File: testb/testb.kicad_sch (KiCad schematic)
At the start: 3 parts

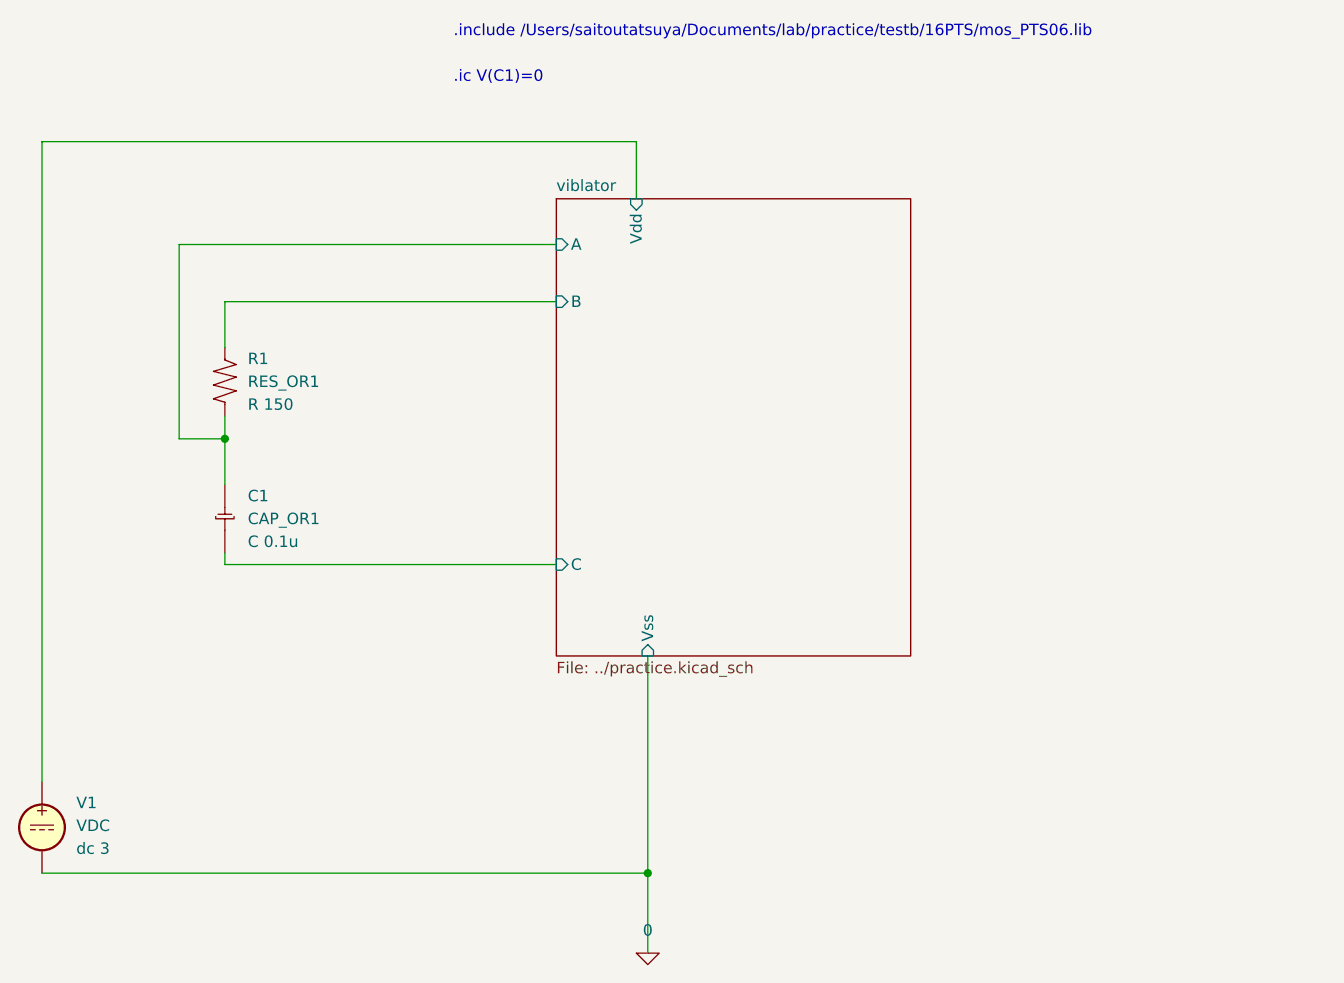
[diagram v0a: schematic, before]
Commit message: 入出力点を双方向に変更
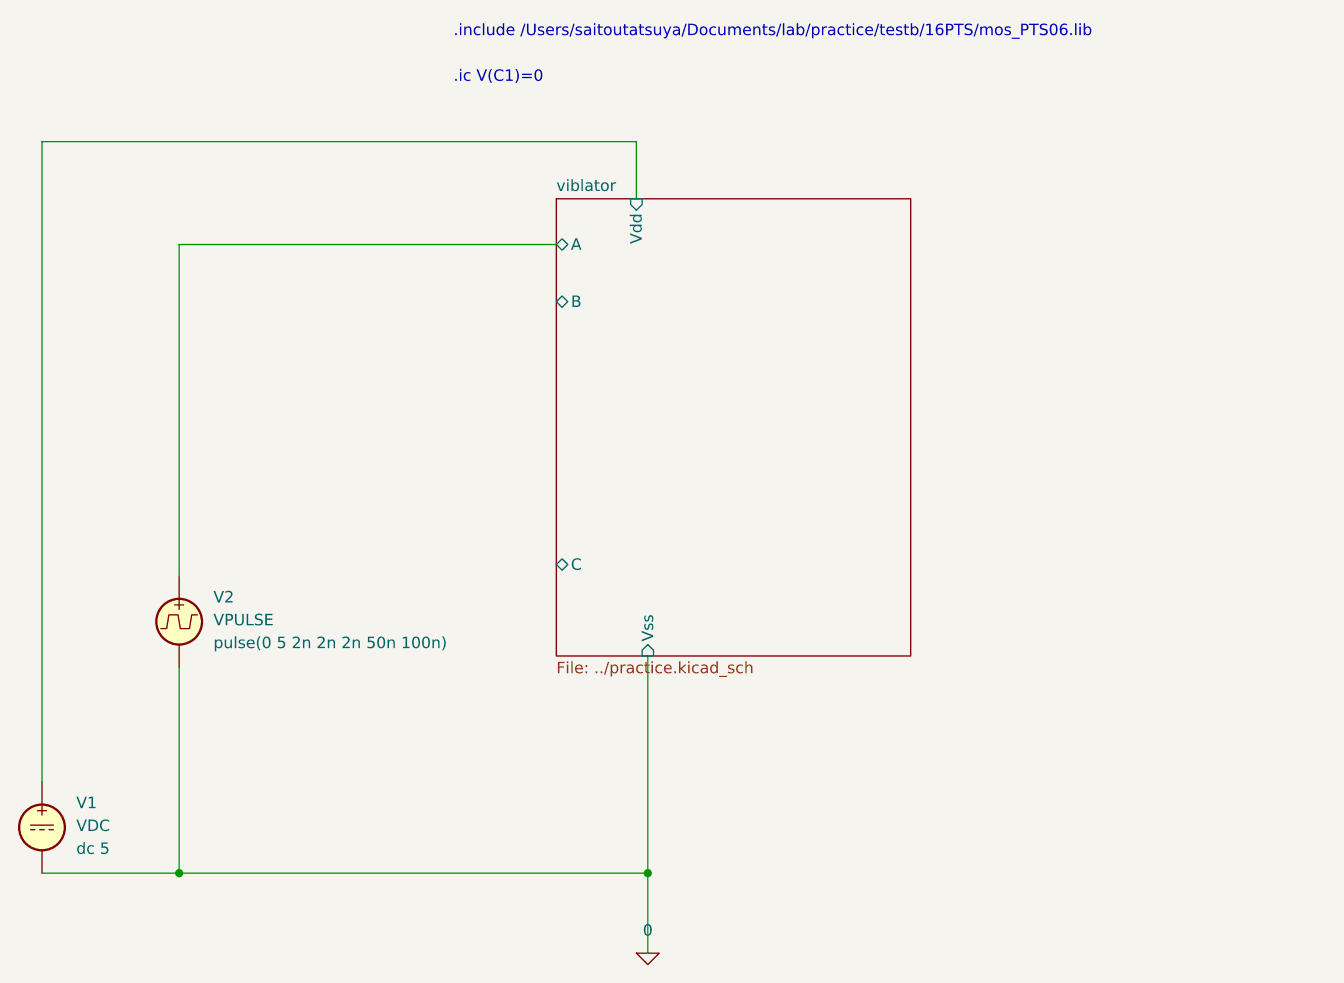
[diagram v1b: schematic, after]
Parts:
- removed C1: CAP_OR1, symbol 0_OR1Symbols:CAP_OR1
- removed R1: RES_OR1, symbol 0_OR1Symbols:RES_OR1
- added V2: VPULSE, symbol Simulation_SPICE:VPULSE
- V1: Spice_Model dc 3 -> dc 5
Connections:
- net 0: now also V2.2
- net viblator/A: now also V2.1
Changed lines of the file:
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@@
   (junction (at 152.4 129.54) (diameter 0) (color 0 0 0 0)
   )
-  (junction (at 105.41 81.28) (diameter 0) (color 0 0 0 0)
+  (junction (at 100.33 129.54) (diameter 0) (color 0 0 0 0)
   )
-  (wire (pts (xy 105.41 95.25) (xy 142.24 95.25))
+  (wire (pts (xy 100.33 106.68) (xy 100.33 129.54))
     (stroke (width 0) (type default) (color 0 0 0 0))
   )
@@
     (stroke (width 0) (type default) (color 0 0 0 0))
   )
-  (wire (pts (xy 152.4 129.54) (xy 152.4 138.43))
+  (wire (pts (xy 100.33 129.54) (xy 152.4 129.54))
     (stroke (width 0) (type default) (color 0 0 0 0))
   )
-  (wire (pts (xy 105.41 66.04) (xy 142.24 66.04))
-    (stroke (width 0) (type default) (color 0 0 0 0))
-  )
-  (wire (pts (xy 100.33 59.69) (xy 100.33 81.28))
+  (wire (pts (xy 152.4 129.54) (xy 152.4 138.43))
     (stroke (width 0) (type default) (color 0 0 0 0))
   )
@@
     (stroke (width 0) (type default) (color 0 0 0 0))
   )
-  (wire (pts (xy 100.33 59.69) (xy 142.24 59.69))
-    (stroke (width 0) (type default) (color 0 0 0 0))
-  )
   (wire (pts (xy 151.13 48.26) (xy 151.13 54.61))
     (stroke (width 0) (type default) (color 0 0 0 0))
   )
-  (wire (pts (xy 105.41 78.74) (xy 105.41 81.28))
+  (wire (pts (xy 85.09 129.54) (xy 100.33 129.54))
     (stroke (width 0) (type default) (color 0 0 0 0))
   )
-  (wire (pts (xy 85.09 129.54) (xy 152.4 129.54))
-    (stroke (width 0) (type default) (color 0 0 0 0))
-  )
-  (wire (pts (xy 105.41 93.98) (xy 105.41 95.25))
-    (stroke (width 0) (type default) (color 0 0 0 0))
-  )
-  (wire (pts (xy 105.41 81.28) (xy 105.41 86.36))
-    (stroke (width 0) (type default) (color 0 0 0 0))
-  )
-  (wire (pts (xy 100.33 81.28) (xy 105.41 81.28))
+  (wire (pts (xy 100.33 96.52) (xy 100.33 59.69))
     (stroke (width 0) (type default) (color 0 0 0 0))
   )
@@
     (stroke (width 0) (type default) (color 0 0 0 0))
   )
-  (wire (pts (xy 105.41 66.04) (xy 105.41 71.12))
+  (wire (pts (xy 100.33 59.69) (xy 142.24 59.69))
     (stroke (width 0) (type default) (color 0 0 0 0))
   )
@@
     (pin "1")
   )
-  (symbol (lib_id "0_OR1Symbols:RES_OR1") (at 105.41 71.12 0) (unit 1)
+  (symbol (lib_id "Simulation_SPICE:VPULSE") (at 100.33 101.6 0) (unit 1)
     (in_bom yes) (on_board yes) (fields_autoplaced)
-    (property "Reference" "R1" (id 0) (at 107.95 72.3899 0)
+    (property "Reference" "V2" (id 0) (at 104.14 98.8701 0)
       (effects (font (size 1.27 1.27)) (justify left))
     )
-    (property "Value" "RES_OR1" (id 1) (at 107.95 74.9299 0)
+    (property "Value" "VPULSE" (id 1) (at 104.14 101.4101 0)
       (effects (font (size 1.27 1.27)) (justify left))
     )
-    (property "Footprint" "" (id 2) (at 106.68 71.12 0)
+    (property "Footprint" "" (id 2) (at 100.33 101.6 0)
       (effects (font (size 1.27 1.27)) hide)
     )
-    (property "Datasheet" "" (id 3) (at 106.68 71.12 0)
+    (property "Datasheet" "~" (id 3) (at 100.33 101.6 0)
       (effects (font (size 1.27 1.27)) hide)
     )
-    (property "Spice_Primitive" "R" (id 4) (at 109.22 80.01 0)
+    (property "Spice_Netlist_Enabled" "Y" (id 4) (at 100.33 101.6 0)
       (effects (font (size 1.27 1.27)) (justify left) hide)
     )
-    (property "Spice_Model" "R 150" (id 5) (at 107.95 77.4699 0)
+    (property "Spice_Primitive" "V" (id 5) (at 100.33 101.6 0)
+      (effects (font (size 1.27 1.27)) (justify left) hide)
+    )
+    (property "Spice_Model" "pulse(0 5 2n 2n 2n 50n 100n)" (id 6) (at 104.14 103.9501 0)
       (effects (font (size 1.27 1.27)) (justify left))
-    )
-    (property "Spice_Netlist_Enabled" "Y" (id 6) (at 109.22 77.47 0)
-      (effects (font (size 1.27 1.27)) (justify left) hide)
     )
     (pin "1")
@@
       (effects (font (size 1.27 1.27)) (justify left) hide)
     )
-    (property "Spice_Model" "dc 3" (id 6) (at 88.9 126.8101 0)
+    (property "Spice_Model" "dc 5" (id 6) (at 88.9 126.8101 0)
       (effects (font (size 1.27 1.27)) (justify left))
-    )
-    (pin "1")
-    (pin "2")
-  )
-  (symbol (lib_id "0_OR1Symbols:CAP_OR1") (at 105.41 86.36 0) (unit 1)
-    (in_bom yes) (on_board yes) (fields_autoplaced)
-    (property "Reference" "C1" (id 0) (at 107.95 87.6299 0)
-      (effects (font (size 1.27 1.27)) (justify left))
-    )
-    (property "Value" "CAP_OR1" (id 1) (at 107.95 90.1699 0)
-      (effects (font (size 1.27 1.27)) (justify left))
-    )
-    (property "Footprint" "" (id 2) (at 104.14 84.582 0)
-      (effects (font (size 1.27 1.27)) hide)
-    )
-    (property "Datasheet" "" (id 3) (at 104.14 84.582 0)
-      (effects (font (size 1.27 1.27)) hide)
-    )
-    (property "Spice_Primitive" "C" (id 4) (at 107.95 96.52 0)
-      (effects (font (size 1.27 1.27)) (justify left) hide)
-    )
-    (property "Spice_Model" "C 0.1u" (id 5) (at 107.95 92.7099 0)
-      (effects (font (size 1.27 1.27)) (justify left))
-    )
-    (property "Spice_Netlist_Enabled" "Y" (id 6) (at 107.95 93.98 0)
-      (effects (font (size 1.27 1.27)) (justify left) hide)
     )
     (pin "1")
@@
       (effects (font (size 1.27 1.27)) (justify left top))
     )
-    (pin "A" input (at 142.24 59.69 180)
-      (effects (font (size 1.27 1.27)) (justify left))
-    )
     (pin "Vdd" input (at 151.13 54.61 90)
       (effects (font (size 1.27 1.27)) (justify right))
-    )
-    (pin "B" input (at 142.24 66.04 180)
-      (effects (font (size 1.27 1.27)) (justify left))
     )
     (pin "Vss" input (at 152.4 105.41 270)
       (effects (font (size 1.27 1.27)) (justify left))
     )
-    (pin "C" input (at 142.24 95.25 180)
+    (pin "A" bidirectional (at 142.24 59.69 180)
+      (effects (font (size 1.27 1.27)) (justify left))
+    )
+    (pin "B" bidirectional (at 142.24 66.04 180)
+      (effects (font (size 1.27 1.27)) (justify left))
+    )
+    (pin "C" bidirectional (at 142.24 95.25 180)
       (effects (font (size 1.27 1.27)) (justify left))
     )
@@
     (path "/03533d21-8bf4-4e20-a4f6-d9e08c36312e"
       (reference "#GND01") (unit 1) (value "0") (footprint "")
-    )
-    (path "/e7907c5a-8ef1-42da-b288-1dd8c5ac9ea4"
-      (reference "C1") (unit 1) (value "CAP_OR1") (footprint "")
     )
     (path "/f9bca915-8d72-4d60-baed-39cb84ddd057/a066ab46-d60f-4bfa-b05f-320c318e2a67"
@@
       (reference "M4") (unit 1) (value "NMOS_OR1") (footprint "")
     )
-    (path "/98714e84-a1de-4723-a587-f743ea5e1539"
-      (reference "R1") (unit 1) (value "RES_OR1") (footprint "")
-    )
     (path "/b717cf87-ea15-43bb-92fa-e84e251c65e1"
       (reference "V1") (unit 1) (value "VDC") (footprint "")
     )
+    (path "/64d5b77c-6954-4017-83df-0c4d5f58903d"
+      (reference "V2") (unit 1) (value "VPULSE") (footprint "")
+    )
   )

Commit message: 19用に合わせた発振回路
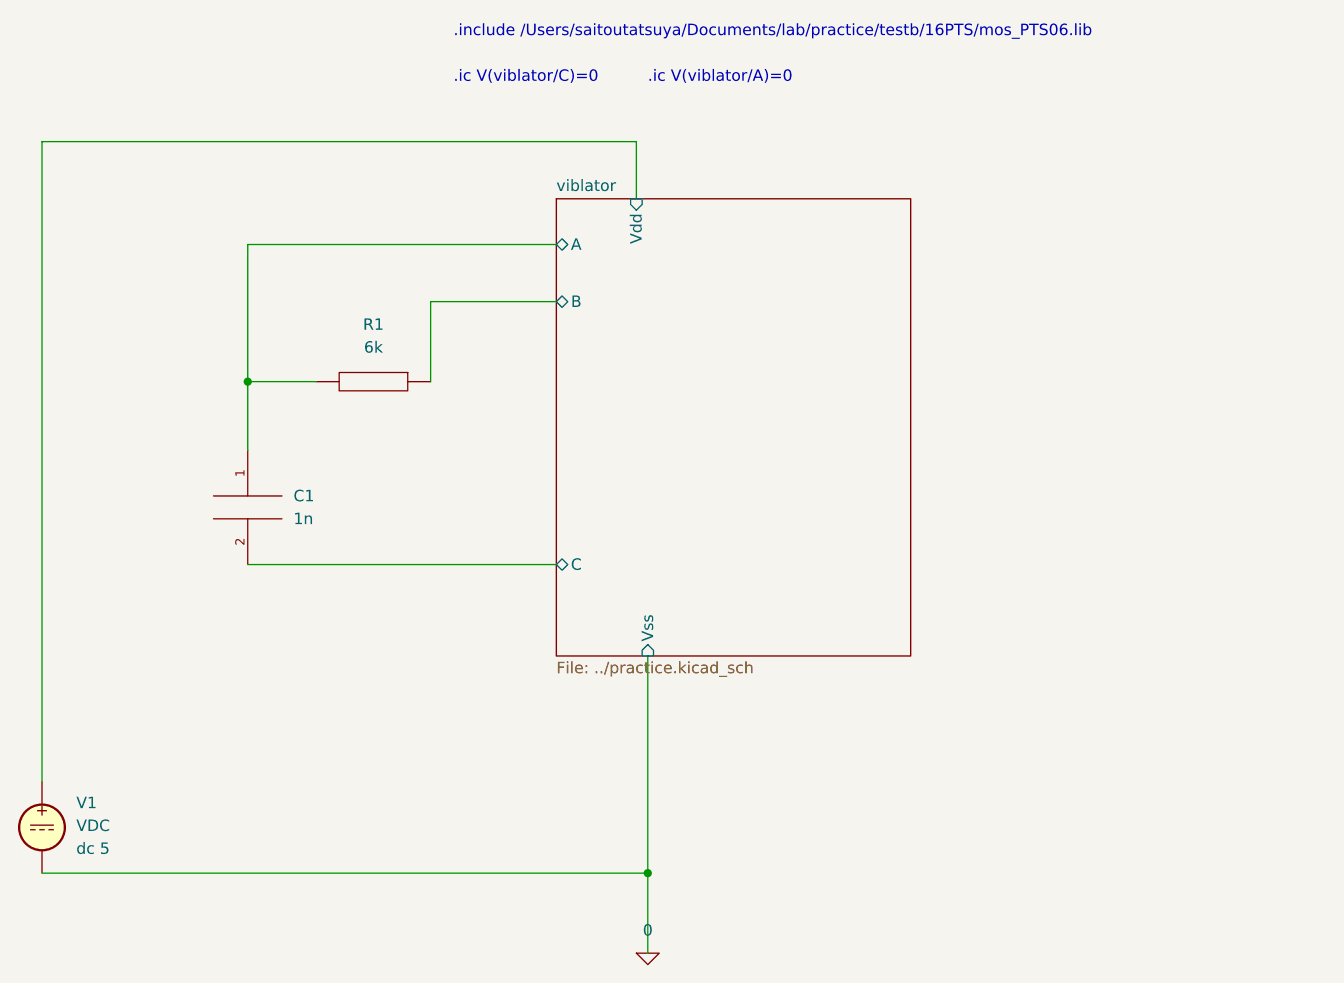
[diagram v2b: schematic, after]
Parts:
- removed V2: VPULSE, symbol Simulation_SPICE:VPULSE
- added C1: 1n, symbol pspice:CAP
- added R1: 6k, symbol pspice:R
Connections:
- net viblator/A: now also C1.1, R1.2
- net viblator/B: now also R1.1
- net viblator/C: now also C1.2
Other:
- note added: ".ic V(viblator/A)=0"
- note added: ".ic V(viblator/C)=0"
- note removed: ".ic V(C1)=0"
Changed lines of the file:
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@@
   (junction (at 152.4 129.54) (diameter 0) (color 0 0 0 0)
   )
-  (junction (at 100.33 129.54) (diameter 0) (color 0 0 0 0)
-  )
-  (wire (pts (xy 100.33 106.68) (xy 100.33 129.54))
-    (stroke (width 0) (type default) (color 0 0 0 0))
+  (junction (at 107.95 74.93) (diameter 0) (color 0 0 0 0)
   )
   (wire (pts (xy 152.4 105.41) (xy 152.4 129.54))
     (stroke (width 0) (type default) (color 0 0 0 0))
   )
-  (wire (pts (xy 100.33 129.54) (xy 152.4 129.54))
+  (wire (pts (xy 85.09 129.54) (xy 152.4 129.54))
     (stroke (width 0) (type default) (color 0 0 0 0))
   )
   (wire (pts (xy 152.4 129.54) (xy 152.4 138.43))
+    (stroke (width 0) (type default) (color 0 0 0 0))
+  )
+  (wire (pts (xy 107.95 95.25) (xy 142.24 95.25))
+    (stroke (width 0) (type default) (color 0 0 0 0))
+  )
+  (wire (pts (xy 107.95 59.69) (xy 142.24 59.69))
+    (stroke (width 0) (type default) (color 0 0 0 0))
+  )
+  (wire (pts (xy 128.27 74.93) (xy 128.27 66.04))
     (stroke (width 0) (type default) (color 0 0 0 0))
   )
@@
     (stroke (width 0) (type default) (color 0 0 0 0))
   )
-  (wire (pts (xy 85.09 129.54) (xy 100.33 129.54))
-    (stroke (width 0) (type default) (color 0 0 0 0))
-  )
-  (wire (pts (xy 100.33 96.52) (xy 100.33 59.69))
+  (wire (pts (xy 107.95 74.93) (xy 107.95 59.69))
     (stroke (width 0) (type default) (color 0 0 0 0))
   )
@@
     (stroke (width 0) (type default) (color 0 0 0 0))
   )
-  (wire (pts (xy 100.33 59.69) (xy 142.24 59.69))
+  (wire (pts (xy 107.95 74.93) (xy 115.57 74.93))
     (stroke (width 0) (type default) (color 0 0 0 0))
   )
-  (text ".ic V(C1)=0" (at 130.81 41.91 0)
+  (wire (pts (xy 128.27 66.04) (xy 142.24 66.04))
+    (stroke (width 0) (type default) (color 0 0 0 0))
+  )
+  (wire (pts (xy 107.95 82.55) (xy 107.95 74.93))
+    (stroke (width 0) (type default) (color 0 0 0 0))
+  )
+  (text ".ic V(viblator/C)=0" (at 130.81 41.91 0)
+    (effects (font (size 1.27 1.27)) (justify left bottom))
+  )
+  (text ".ic V(viblator/A)=0" (at 152.4 41.91 0)
     (effects (font (size 1.27 1.27)) (justify left bottom))
   )
@@
     (pin "1")
   )
-  (symbol (lib_id "Simulation_SPICE:VPULSE") (at 100.33 101.6 0) (unit 1)
+  (symbol (lib_id "pspice:R") (at 121.92 74.93 270) (unit 1)
     (in_bom yes) (on_board yes) (fields_autoplaced)
-    (property "Reference" "V2" (id 0) (at 104.14 98.8701 0)
+    (property "Reference" "R1" (id 0) (at 121.92 68.58 90))
+    (property "Value" "6k" (id 1) (at 121.92 71.12 90))
+    (property "Footprint" "" (id 2) (at 121.92 74.93 0)
+      (effects (font (size 1.27 1.27)) hide)
+    )
+    (property "Datasheet" "~" (id 3) (at 121.92 74.93 0)
+      (effects (font (size 1.27 1.27)) hide)
+    )
+    (pin "1")
+    (pin "2")
+  )
+  (symbol (lib_id "pspice:CAP") (at 107.95 88.9 0) (unit 1)
+    (in_bom yes) (on_board yes) (fields_autoplaced)
+    (property "Reference" "C1" (id 0) (at 113.03 87.6299 0)
       (effects (font (size 1.27 1.27)) (justify left))
     )
-    (property "Value" "VPULSE" (id 1) (at 104.14 101.4101 0)
+    (property "Value" "1n" (id 1) (at 113.03 90.1699 0)
       (effects (font (size 1.27 1.27)) (justify left))
     )
-    (property "Footprint" "" (id 2) (at 100.33 101.6 0)
+    (property "Footprint" "" (id 2) (at 107.95 88.9 0)
       (effects (font (size 1.27 1.27)) hide)
     )
-    (property "Datasheet" "~" (id 3) (at 100.33 101.6 0)
+    (property "Datasheet" "~" (id 3) (at 107.95 88.9 0)
       (effects (font (size 1.27 1.27)) hide)
-    )
-    (property "Spice_Netlist_Enabled" "Y" (id 4) (at 100.33 101.6 0)
-      (effects (font (size 1.27 1.27)) (justify left) hide)
-    )
-    (property "Spice_Primitive" "V" (id 5) (at 100.33 101.6 0)
-      (effects (font (size 1.27 1.27)) (justify left) hide)
-    )
-    (property "Spice_Model" "pulse(0 5 2n 2n 2n 50n 100n)" (id 6) (at 104.14 103.9501 0)
-      (effects (font (size 1.27 1.27)) (justify left))
     )
     (pin "1")
@@
       (reference "#GND01") (unit 1) (value "0") (footprint "")
     )
+    (path "/3b89403b-2c4c-45f6-bc33-71f71e58fc2e"
+      (reference "C1") (unit 1) (value "1n") (footprint "")
+    )
     (path "/f9bca915-8d72-4d60-baed-39cb84ddd057/a066ab46-d60f-4bfa-b05f-320c318e2a67"
       (reference "M1") (unit 1) (value "PMOS_OR1") (footprint "")
@@
       (reference "M4") (unit 1) (value "NMOS_OR1") (footprint "")
     )
+    (path "/2cfb77fc-63f8-4888-94b3-0e86a309ac26"
+      (reference "R1") (unit 1) (value "6k") (footprint "")
+    )
     (path "/b717cf87-ea15-43bb-92fa-e84e251c65e1"
       (reference "V1") (unit 1) (value "VDC") (footprint "")
     )
-    (path "/64d5b77c-6954-4017-83df-0c4d5f58903d"
-      (reference "V2") (unit 1) (value "VPULSE") (footprint "")
-    )
   )
